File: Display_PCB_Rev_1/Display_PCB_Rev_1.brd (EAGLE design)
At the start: 76.5 x 53 mm, 9 parts, among them J1 71430-015

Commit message: Ripped up old differential signal routes, and added in start of new route with smaller trace width.
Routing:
- net RXIN0_N: track 97.9 -> 12.3 mm
- net RXIN0_P: track 67.5 -> 6.81 mm
- net RXIN1_N: track 42.2 -> 0.00 mm
- net RXIN2_N: track 35.3 -> 0.00 mm
- net CLK_N: track 21.0 -> 0.00 mm
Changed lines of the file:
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@@
 <setting verticaltext="up"/>
 </settings>
-<grid distance="0.5" unitdist="mm" unit="mm" style="dots" multiple="1" display="yes" altdistance="0.25" altunitdist="mm" altunit="mm"/>
+<grid distance="0.0625" unitdist="mm" unit="mm" style="dots" multiple="1" display="yes" altdistance="0.0625" altunitdist="mm" altunit="mm"/>
 <layers>
 <layer number="1" name="Top" color="4" fill="1" visible="yes" active="yes"/>
@@
 &lt;br&gt;Min width/Spacing: 5/5mil
 &lt;br&gt;Min diameter of finished hole 12mil</description>
-<param name="layerSetup" value="(1*2*3*16)"/>
+<param name="layerSetup" value="(1*2+3*16)"/>
 <param name="mtCopper" value="0.035mm 0.035mm 0.035mm 0.035mm 0.035mm 0.035mm 0.035mm 0.035mm 0.035mm 0.035mm 0.035mm 0.035mm 0.035mm 0.035mm 0.0175mm 0.035mm"/>
 <param name="mtIsolate" value="0.48mm 0.49mm 0.48mm 0.15mm 0.2mm 0.15mm 0.2mm 0.15mm 0.2mm 0.15mm 0.2mm 0.15mm 0.2mm 0.15mm 0.2mm"/>
@@
 <wire x1="83.5" y1="65" x2="82.679284375" y2="64.355996875" width="0.254" layer="2"/>
 <wire x1="82.679284375" y1="64.355996875" x2="80.16164375" y2="61.83835625" width="0.254" layer="2"/>
-<wire x1="80.161646875" y1="61.838353125" x2="63.59469375" y2="45.2714" width="0.254" layer="2"/>
-<wire x1="63.59469375" y1="45.2714" x2="26" y2="45.2714" width="0.254" layer="2"/>
-<wire x1="19.7640125" y1="45.471975" x2="19.706340625" y2="45.58731875" width="0" layer="19" extent="1-16"/>
-<wire x1="19.706340625" y1="45.58731875" x2="18.0721" y2="45.8274125" width="0" layer="19" curve="85.401073" extent="1-16"/>
-<wire x1="18.0721" y1="45.8274125" x2="18" y2="45.395" width="0" layer="19" extent="1-16"/>
-<wire x1="19.861803125" y1="44.72360625" x2="19.816228125" y2="44.63245625" width="0" layer="19" extent="1-16"/>
-<wire x1="19.816228125" y1="44.63245625" x2="18.86754375" y2="44.316228125" width="0" layer="19" curve="-90" extent="1-16"/>
-<wire x1="18.86754375" y1="44.316228125" x2="18.5" y2="44.5" width="0" layer="19" extent="1-16"/>
-<wire x1="80.161646875" y1="61.838353125" x2="80.16164375" y2="61.83835625" width="0" layer="19" extent="2-2"/>
 <wire x1="23.06" y1="78.27" x2="80.16164375" y2="61.83835625" width="0" layer="19" extent="1-2"/>
-<wire x1="26" y1="45.2714" x2="22" y2="39.5" width="0" layer="19" extent="1-16"/>
-<wire x1="22" y1="39.5" x2="18" y2="45.395" width="0" layer="19" extent="1-16"/>
-<wire x1="18" y1="45.395" x2="15.5" y2="45.395" width="0.254" layer="2"/>
-<wire x1="15.5" y1="45.395" x2="15.5" y2="35.5" width="0.254" layer="2"/>
-<wire x1="15.5" y1="35.5" x2="22" y2="35.5" width="0.254" layer="2"/>
-<wire x1="22" y1="35.5" x2="22" y2="45" width="0.254" layer="2"/>
-<wire x1="22" y1="45" x2="26" y2="45.2714" width="0" layer="19" extent="1-16"/>
+<wire x1="18" y1="45.395" x2="18.4575" y2="45.395" width="0.127" layer="2"/>
+<wire x1="18.4575" y1="45.395" x2="18.8125" y2="45.75" width="0.127" layer="2"/>
+<wire x1="18.8125" y1="45.75" x2="19.4375" y2="45.75" width="0.127" layer="2"/>
+<wire x1="19.4375" y1="45.75" x2="20.25" y2="44.9375" width="0.127" layer="2"/>
+<wire x1="20.25" y1="44.9375" x2="21.3125" y2="44.9375" width="0.127" layer="2"/>
+<wire x1="21.3125" y1="44.9375" x2="23.06" y2="78.27" width="0" layer="19" extent="1-16"/>
 </signal>
 <signal name="RXIN1_N">
@@
 <contactref element="JP3" pad="4"/>
 <wire x1="25.6" y1="78.27" x2="87" y2="68" width="0" layer="19" extent="1-1"/>
-<wire x1="18" y1="50.195" x2="14.5" y2="50.195" width="0.254" layer="2"/>
-<wire x1="14.5" y1="50.195" x2="14.5" y2="35" width="0.254" layer="2"/>
-<wire x1="14.5" y1="35" x2="23" y2="35" width="0.254" layer="2"/>
-<wire x1="23" y1="35" x2="23" y2="50" width="0.254" layer="2"/>
-<wire x1="23" y1="50" x2="25.6" y2="78.27" width="0" layer="19" extent="1-16"/>
+<wire x1="18" y1="50.195" x2="25.6" y2="78.27" width="0" layer="19" extent="1-1"/>
 </signal>
 <signal name="RXIN0_P">
@@
 <wire x1="83.5" y1="66" x2="82.350628125" y2="64.673915625" width="0.254" layer="2"/>
 <wire x1="82.350628125" y1="64.673915625" x2="79.83835625" y2="62.16164375" width="0.254" layer="2"/>
-<wire x1="79.838353125" y1="62.161646875" x2="63.40530625" y2="45.7286" width="0.254" layer="2"/>
-<wire x1="63.40530625" y1="45.7286" x2="26" y2="45.7286" width="0.254" layer="2"/>
-<wire x1="26" y1="45.7286" x2="20.9336" y2="45.795" width="0" layer="19" extent="1-16"/>
-<wire x1="20.9336" y1="45.795" x2="20.35" y2="45.795" width="0" layer="19" extent="1-16"/>
-<wire x1="79.838353125" y1="62.161646875" x2="79.83835625" y2="62.16164375" width="0" layer="19" extent="2-2"/>
 <wire x1="23.06" y1="75.73" x2="79.83835625" y2="62.16164375" width="0" layer="19" extent="1-2"/>
+<wire x1="20.35" y1="45.795" x2="23.06" y2="75.73" width="0" layer="19" extent="1-1"/>
 </signal>
 <signal name="RXIN1_P">
@@
 <contactref element="JP3" pad="10"/>
 <wire x1="33.22" y1="78.27" x2="87" y2="70" width="0" layer="19" extent="1-1"/>
-<wire x1="16.85" y1="60.595" x2="14.5" y2="60.595" width="0.254" layer="2"/>
-<wire x1="14.5" y1="60.595" x2="14.5" y2="73" width="0.254" layer="2"/>
-<wire x1="14.5" y1="73" x2="23.5" y2="73" width="0.254" layer="2"/>
-<wire x1="23.5" y1="73" x2="23.5" y2="61.5" width="0.254" layer="2"/>
-<wire x1="23.5" y1="61.5" x2="33.22" y2="78.27" width="0" layer="19" extent="1-16"/>
+<wire x1="16.85" y1="60.595" x2="33.22" y2="78.27" width="0" layer="19" extent="1-1"/>
 </signal>
 <signal name="RXIN2_P">
@@
 <contactref element="JP3" pad="12"/>
 <wire x1="35.76" y1="78.27" x2="87" y2="74" width="0" layer="19" extent="1-1"/>
-<wire x1="16.85" y1="65.395" x2="15.5" y2="65.395" width="0.254" layer="2"/>
-<wire x1="15.5" y1="65.395" x2="15.5" y2="72.5" width="0.254" layer="2"/>
-<wire x1="15.5" y1="72.5" x2="22.5" y2="72.5" width="0.254" layer="2"/>
-<wire x1="22.5" y1="72.5" x2="22.5" y2="67" width="0.254" layer="2"/>
-<wire x1="22.5" y1="67" x2="35.76" y2="78.27" width="0" layer="19" extent="1-16"/>
+<wire x1="16.85" y1="65.395" x2="35.76" y2="78.27" width="0" layer="19" extent="1-1"/>
 </signal>
 <signal name="CLK_P">
@@
 <signal name="N$4">
 </signal>
+<signal name="N$2">
+</signal>
 </signals>

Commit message: First Diff Pair VHDCI
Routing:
- net RXIN0_P: track 6.81 -> 67.9 mm
- net RXIN0_N: track 12.3 -> 73.1 mm
- net RXIN1_N: track 0.00 -> 4.41 mm
- net RXIN1_P: track 0.00 -> 1.48 mm
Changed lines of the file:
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@@
 <contactref element="J1" pad="41"/>
 <contactref element="JP3" pad="2"/>
-<wire x1="87" y1="66" x2="86" y2="65" width="0.254" layer="2"/>
-<wire x1="86" y1="65" x2="83.5" y2="65" width="0.254" layer="2"/>
-<wire x1="83.5" y1="65" x2="82.679284375" y2="64.355996875" width="0.254" layer="2"/>
-<wire x1="82.679284375" y1="64.355996875" x2="80.16164375" y2="61.83835625" width="0.254" layer="2"/>
-<wire x1="23.06" y1="78.27" x2="80.16164375" y2="61.83835625" width="0" layer="19" extent="1-2"/>
+<wire x1="86" y1="65" x2="83.5" y2="65" width="0" layer="19" extent="1-16"/>
+<wire x1="83.5" y1="65" x2="82.679284375" y2="64.355996875" width="0" layer="19" extent="1-16"/>
+<wire x1="82.679284375" y1="64.355996875" x2="80.16164375" y2="61.83835625" width="0" layer="19" extent="1-16"/>
 <wire x1="18" y1="45.395" x2="18.4575" y2="45.395" width="0.127" layer="2"/>
 <wire x1="18.4575" y1="45.395" x2="18.8125" y2="45.75" width="0.127" layer="2"/>
@@
 <wire x1="19.4375" y1="45.75" x2="20.25" y2="44.9375" width="0.127" layer="2"/>
 <wire x1="20.25" y1="44.9375" x2="21.3125" y2="44.9375" width="0.127" layer="2"/>
-<wire x1="21.3125" y1="44.9375" x2="23.06" y2="78.27" width="0" layer="19" extent="1-16"/>
+<wire x1="23.06" y1="78.27" x2="80.16164375" y2="61.83835625" width="0" layer="19" extent="1-2"/>
+<wire x1="21.3125" y1="44.9375" x2="21.875" y2="45.123" width="0.127" layer="2"/>
+<wire x1="21.875" y1="45.123" x2="23.06" y2="78.27" width="0" layer="19" extent="1-16"/>
+<wire x1="87" y1="66" x2="86.0625" y2="65" width="0.127" layer="2"/>
+<wire x1="86.0625" y1="65" x2="83.3125" y2="65.0625" width="0.127" layer="2"/>
+<wire x1="83.3125" y1="65.0625" x2="82.7602375" y2="65.182125" width="0.127" layer="2"/>
+<wire x1="82.7602375" y1="65.182125" x2="21.9148625" y2="45.12941875" width="0.127" layer="2"/>
+<wire x1="21.9148625" y1="45.12941875" x2="23.06" y2="78.27" width="0" layer="19" extent="1-16"/>
 </signal>
 <signal name="RXIN1_N">
@@
 <contactref element="JP3" pad="4"/>
 <wire x1="25.6" y1="78.27" x2="87" y2="68" width="0" layer="19" extent="1-1"/>
-<wire x1="18" y1="50.195" x2="25.6" y2="78.27" width="0" layer="19" extent="1-1"/>
+<wire x1="18" y1="50.195" x2="18.9375" y2="50.625" width="0.127" layer="2"/>
+<wire x1="18.9375" y1="50.625" x2="19.4375" y2="50.625" width="0.127" layer="2"/>
+<wire x1="19.4375" y1="50.625" x2="20.0625" y2="49.8125" width="0.127" layer="2"/>
+<wire x1="20.0625" y1="49.8125" x2="21.375" y2="49.8125" width="0.127" layer="2"/>
+<wire x1="21.375" y1="49.8125" x2="21.8125" y2="50.123" width="0.127" layer="2"/>
+<wire x1="21.8125" y1="50.123" x2="25.6" y2="78.27" width="0" layer="19" extent="1-16"/>
 </signal>
 <signal name="RXIN0_P">
@@
 <contactref element="J1" pad="7"/>
 <contactref element="JP3" pad="1"/>
-<wire x1="85" y1="66" x2="83.5" y2="66" width="0.254" layer="2"/>
-<wire x1="83.5" y1="66" x2="82.350628125" y2="64.673915625" width="0.254" layer="2"/>
-<wire x1="82.350628125" y1="64.673915625" x2="79.83835625" y2="62.16164375" width="0.254" layer="2"/>
-<wire x1="23.06" y1="75.73" x2="79.83835625" y2="62.16164375" width="0" layer="19" extent="1-2"/>
-<wire x1="20.35" y1="45.795" x2="23.06" y2="75.73" width="0" layer="19" extent="1-1"/>
+<wire x1="20.35" y1="45.795" x2="21.8125" y2="45.4395" width="0.127" layer="2"/>
+<wire x1="21.8125" y1="45.4395" x2="23.06" y2="75.73" width="0" layer="19" extent="1-2"/>
+<wire x1="85" y1="66" x2="82.688134375" y2="65.48830625" width="0.127" layer="2"/>
+<wire x1="82.688134375" y1="65.48830625" x2="21.8351375" y2="45.43308125" width="0.127" layer="2"/>
+<wire x1="21.8351375" y1="45.43308125" x2="23.06" y2="75.73" width="0" layer="19" extent="1-16"/>
 </signal>
 <signal name="RXIN1_P">
@@
 <contactref element="JP3" pad="3"/>
 <wire x1="25.6" y1="75.73" x2="85" y2="68" width="0" layer="19" extent="1-1"/>
-<wire x1="20.35" y1="50.595" x2="25.6" y2="75.73" width="0" layer="19" extent="1-1"/>
+<wire x1="20.35" y1="50.595" x2="21.8125" y2="50.377" width="0.127" layer="2"/>
+<wire x1="21.8125" y1="50.377" x2="25.6" y2="75.73" width="0" layer="19" extent="1-16"/>
 </signal>
 <signal name="RXIN2_N">

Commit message: VHDCI diff signals wired, not matched lengths though
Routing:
- net CLK_N: track 0.00 -> 72.4 mm
- net RXIN2_N: track 0.00 -> 72.2 mm
- net RXIN1_N: track 4.41 -> 72.3 mm
- net RXIN2_P: track 0.00 -> 66.5 mm
- net CLK_P: track 0.00 -> 66.4 mm
- net RXIN1_P: track 1.48 -> 67.1 mm
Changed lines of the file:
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@@
 <contactref element="J1" pad="47"/>
 <contactref element="JP3" pad="4"/>
-<wire x1="25.6" y1="78.27" x2="87" y2="68" width="0" layer="19" extent="1-1"/>
 <wire x1="18" y1="50.195" x2="18.9375" y2="50.625" width="0.127" layer="2"/>
 <wire x1="18.9375" y1="50.625" x2="19.4375" y2="50.625" width="0.127" layer="2"/>
 <wire x1="19.4375" y1="50.625" x2="20.0625" y2="49.8125" width="0.127" layer="2"/>
 <wire x1="20.0625" y1="49.8125" x2="21.375" y2="49.8125" width="0.127" layer="2"/>
-<wire x1="21.375" y1="49.8125" x2="21.8125" y2="50.123" width="0.127" layer="2"/>
-<wire x1="21.8125" y1="50.123" x2="25.6" y2="78.27" width="0" layer="19" extent="1-16"/>
+<wire x1="21.375" y1="49.8125" x2="21.875" y2="50.123" width="0.127" layer="2"/>
+<wire x1="21.875" y1="50.123" x2="25.6" y2="78.27" width="0" layer="19" extent="1-16"/>
+<wire x1="87" y1="68" x2="86" y2="67" width="0.127" layer="2"/>
+<wire x1="86" y1="67" x2="83.125" y2="67" width="0.127" layer="2"/>
+<wire x1="83.125" y1="67" x2="82.137215625" y2="67.058996875" width="0.127" layer="2"/>
+<wire x1="82.137215625" y1="67.058996875" x2="21.909453125" y2="50.127765625" width="0.127" layer="2"/>
+<wire x1="21.909453125" y1="50.127765625" x2="25.6" y2="78.27" width="0" layer="19" extent="1-16"/>
 </signal>
 <signal name="RXIN0_P">
@@
 <contactref element="J1" pad="13"/>
 <contactref element="JP3" pad="3"/>
-<wire x1="25.6" y1="75.73" x2="85" y2="68" width="0" layer="19" extent="1-1"/>
 <wire x1="20.35" y1="50.595" x2="21.8125" y2="50.377" width="0.127" layer="2"/>
 <wire x1="21.8125" y1="50.377" x2="25.6" y2="75.73" width="0" layer="19" extent="1-16"/>
+<wire x1="85" y1="68" x2="82.0491125" y2="67.36055625" width="0.127" layer="2"/>
+<wire x1="82.0491125" y1="67.36055625" x2="21.778046875" y2="50.372234375" width="0.127" layer="2"/>
+<wire x1="21.778046875" y1="50.372234375" x2="25.6" y2="75.73" width="0" layer="19" extent="1-16"/>
 </signal>
 <signal name="RXIN2_N">
@@
 <contactref element="J1" pad="60"/>
 <contactref element="JP3" pad="10"/>
-<wire x1="33.22" y1="78.27" x2="87" y2="70" width="0" layer="19" extent="1-1"/>
-<wire x1="16.85" y1="60.595" x2="33.22" y2="78.27" width="0" layer="19" extent="1-1"/>
+<wire x1="16.85" y1="60.595" x2="18.5625" y2="60.4375" width="0.127" layer="2"/>
+<wire x1="18.5625" y1="60.4375" x2="19.5625" y2="60.0625" width="0.127" layer="2"/>
+<wire x1="19.5625" y1="60.0625" x2="20.0625" y2="59.4375" width="0.127" layer="2"/>
+<wire x1="20.0625" y1="59.4375" x2="20.9375" y2="59.4375" width="0.127" layer="2"/>
+<wire x1="20.9375" y1="59.4375" x2="21.8125" y2="60.625" width="0.127" layer="2"/>
+<wire x1="21.8125" y1="60.625" x2="22.195446875" y2="60.70683125" width="0.127" layer="2"/>
+<wire x1="22.195446875" y1="60.70683125" x2="33.22" y2="78.27" width="0" layer="19" extent="1-16"/>
+<wire x1="87" y1="70" x2="86" y2="68.9375" width="0.127" layer="2"/>
+<wire x1="86" y1="68.9375" x2="83.3125" y2="68.9375" width="0.127" layer="2"/>
+<wire x1="83.3125" y1="68.9375" x2="82.125" y2="68.998" width="0.127" layer="2"/>
+<wire x1="82.125" y1="68.998" x2="22.142053125" y2="60.686653125" width="0.127" layer="2"/>
+<wire x1="22.142053125" y1="60.686653125" x2="33.22" y2="78.27" width="0" layer="19" extent="1-16"/>
 </signal>
 <signal name="RXIN2_P">
@@
 <contactref element="J1" pad="26"/>
 <contactref element="JP3" pad="9"/>
-<wire x1="33.22" y1="75.73" x2="85" y2="70" width="0" layer="19" extent="1-1"/>
-<wire x1="19.2" y1="60.995" x2="33.22" y2="75.73" width="0" layer="19" extent="1-1"/>
+<wire x1="19.2" y1="60.995" x2="22.192596875" y2="61.001896875" width="0.127" layer="2"/>
+<wire x1="22.192596875" y1="61.001896875" x2="33.22" y2="75.73" width="0" layer="19" extent="1-16"/>
+<wire x1="85" y1="70" x2="82.125" y2="69.3145" width="0.127" layer="2"/>
+<wire x1="82.125" y1="69.3145" x2="22.16979375" y2="61.000759375" width="0.127" layer="2"/>
+<wire x1="22.16979375" y1="61.000759375" x2="33.22" y2="75.73" width="0" layer="19" extent="1-16"/>
 </signal>
 <signal name="CLK_N">
@@
 <contactref element="J1" pad="66"/>
 <contactref element="JP3" pad="12"/>
-<wire x1="35.76" y1="78.27" x2="87" y2="74" width="0" layer="19" extent="1-1"/>
-<wire x1="16.85" y1="65.395" x2="35.76" y2="78.27" width="0" layer="19" extent="1-1"/>
+<wire x1="16.85" y1="65.395" x2="18.4375" y2="65.4375" width="0.127" layer="2"/>
+<wire x1="18.4375" y1="65.4375" x2="18.9375" y2="64.9375" width="0.127" layer="2"/>
+<wire x1="18.9375" y1="64.9375" x2="19.5" y2="64.9375" width="0.127" layer="2"/>
+<wire x1="19.5" y1="64.9375" x2="20.1875" y2="64.1875" width="0.127" layer="2"/>
+<wire x1="20.1875" y1="64.1875" x2="20.8125" y2="64.1875" width="0.127" layer="2"/>
+<wire x1="20.8125" y1="64.1875" x2="21.8125" y2="65.5625" width="0.127" layer="2"/>
+<wire x1="21.8125" y1="65.5625" x2="22.300025" y2="65.57076875" width="0.127" layer="2"/>
+<wire x1="87" y1="74" x2="86.125" y2="73" width="0.127" layer="2"/>
+<wire x1="86.125" y1="73" x2="83.375" y2="73" width="0.127" layer="2"/>
+<wire x1="83.375" y1="73" x2="82.5" y2="73.0605" width="0.127" layer="2"/>
+<wire x1="82.5" y1="73.0605" x2="35.76" y2="78.27" width="0" layer="19" extent="1-16"/>
+<wire x1="22.300025" y1="65.57076875" x2="82.578553125" y2="73.06151875" width="0.127" layer="2"/>
+<wire x1="82.578553125" y1="73.06151875" x2="35.76" y2="78.27" width="0" layer="19" extent="1-16"/>
 </signal>
 <signal name="CLK_P">
@@
 <contactref element="J1" pad="32"/>
 <contactref element="JP3" pad="11"/>
-<wire x1="35.76" y1="75.73" x2="85" y2="74" width="0" layer="19" extent="1-1"/>
-<wire x1="19.2" y1="65.795" x2="35.76" y2="75.73" width="0" layer="19" extent="1-1"/>
+<wire x1="19.2" y1="65.795" x2="22.314371875" y2="65.876984375" width="0.127" layer="2"/>
+<wire x1="85" y1="74" x2="82.5" y2="73.377" width="0.127" layer="2"/>
+<wire x1="82.5" y1="73.377" x2="35.76" y2="75.73" width="0" layer="19" extent="1-16"/>
+<wire x1="22.314371875" y1="65.876984375" x2="82.547075" y2="73.376059375" width="0.127" layer="2"/>
+<wire x1="82.547075" y1="73.376059375" x2="35.76" y2="75.73" width="0" layer="19" extent="1-16"/>
 </signal>
 <signal name="VCC_12">

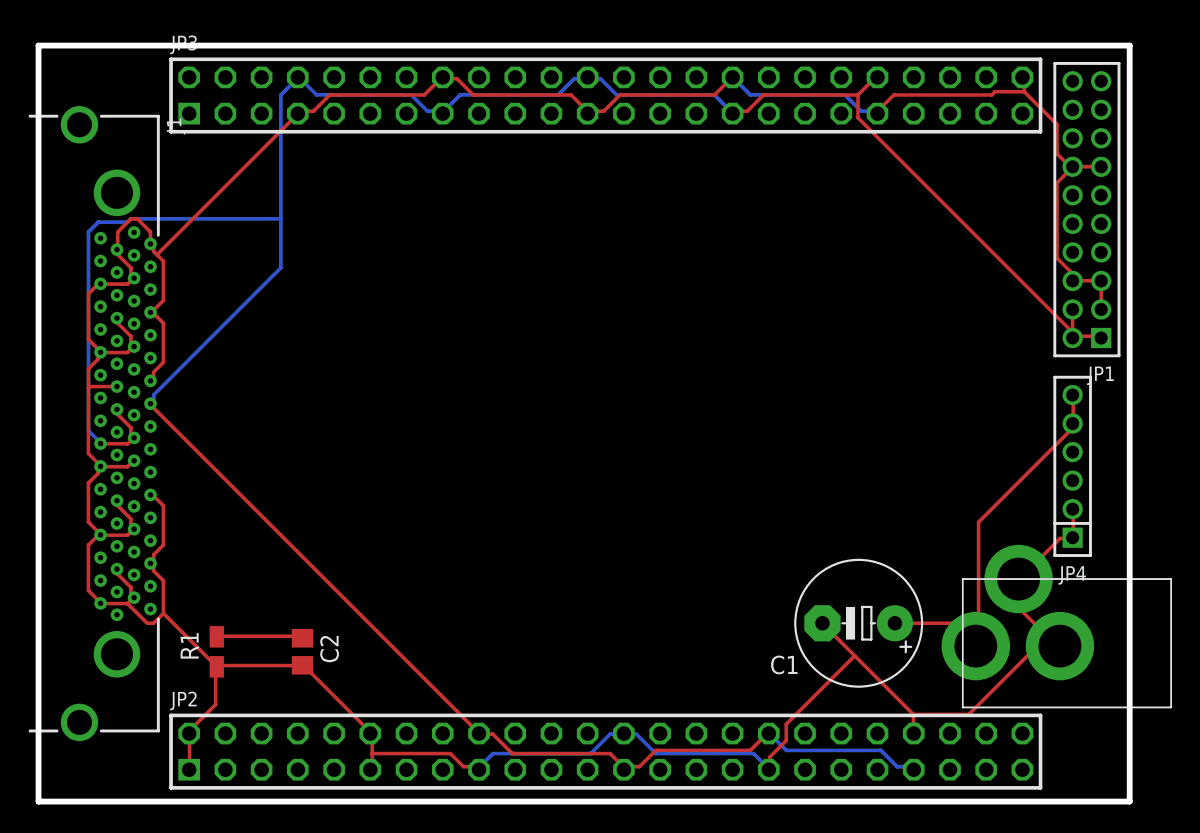
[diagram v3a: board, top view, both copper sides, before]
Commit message: VHDCI Connector finished and matched length
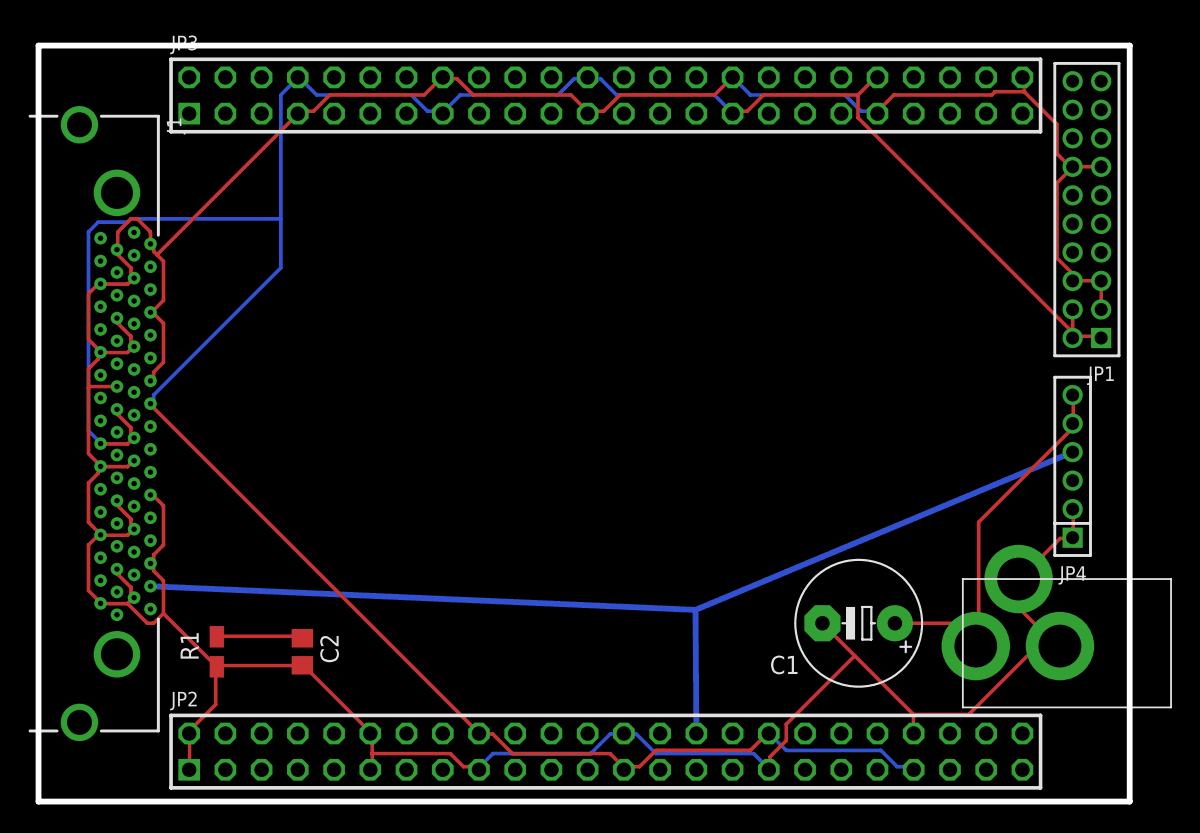
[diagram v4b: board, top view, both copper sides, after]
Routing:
- net DE: track 0.00 -> 75.6 mm
- net CLK_P: track 66.4 -> 71.3 mm
- net RXIN2_P: track 66.5 -> 71.3 mm
- net RXIN1_P: track 67.1 -> 71.5 mm
- net RXIN0_P: track 67.9 -> 71.8 mm
- net RXIN1_N: track 72.3 -> 73.0 mm
- net RXIN2_N: track 72.2 -> 72.9 mm
- net CLK_N: track 72.4 -> 73.0 mm
